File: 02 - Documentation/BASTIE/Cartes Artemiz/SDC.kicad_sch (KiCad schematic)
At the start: 28 parts, among them K1 NO Relay, K10 NO Relay, K11 NO Relay, K2 NO Relay, K3 NO Relay, K4 NO Relay, K5 NC Relay, K6 NO Relay, K7 NO Relay, K8 NO Relay, K9 NO Relay, Q1 NMOS SQ2348ES-T1_GE3, Q2 NMOS SQ2348ES-T1_GE3, Q3 NMOS SQ2348ES-T1_GE3, Q4 NMOS SQ2348ES-T1_GE3, Q5 NMOS SQ2348ES-T1_GE3, Q6 NMOS SQ2348ES-T1_GE3, Q7 NMOS SQ2348ES-T1_GE3, U1 ADG417BR, U2 ADG417BR, U3 ADG417BR, U4 ADG417BR, U5 ADG417BR, U6 ADG417BR, U7 ADG417BR, U8 ADG417BR

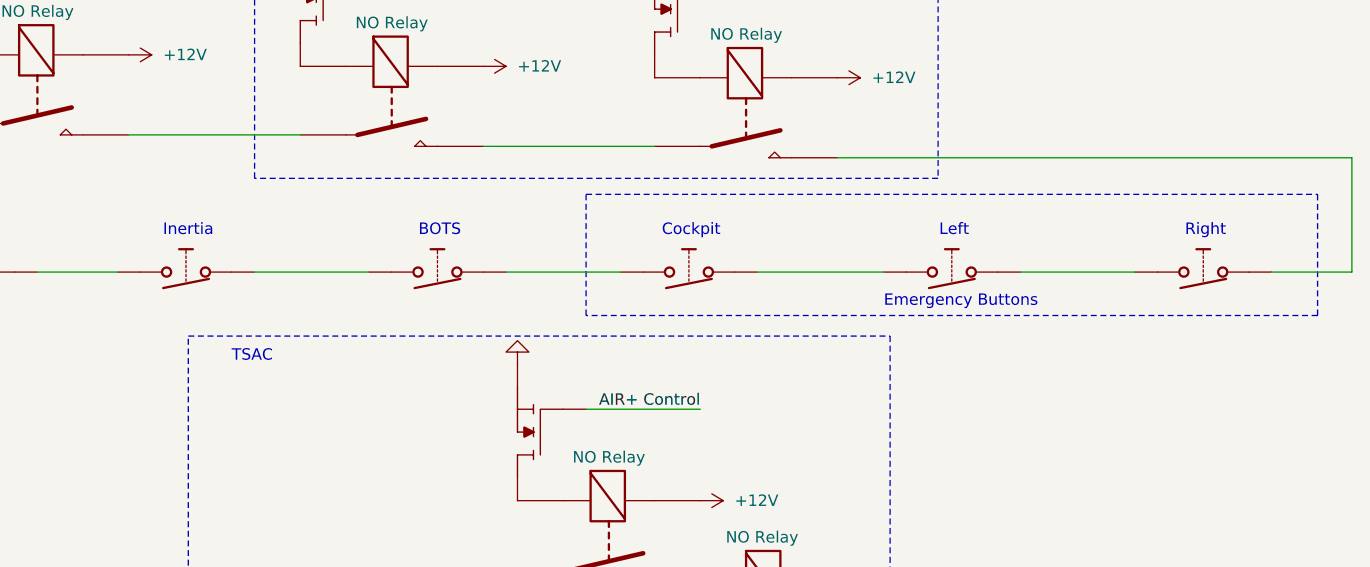
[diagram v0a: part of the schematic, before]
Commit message: Modifications de cartes pour l'ESF
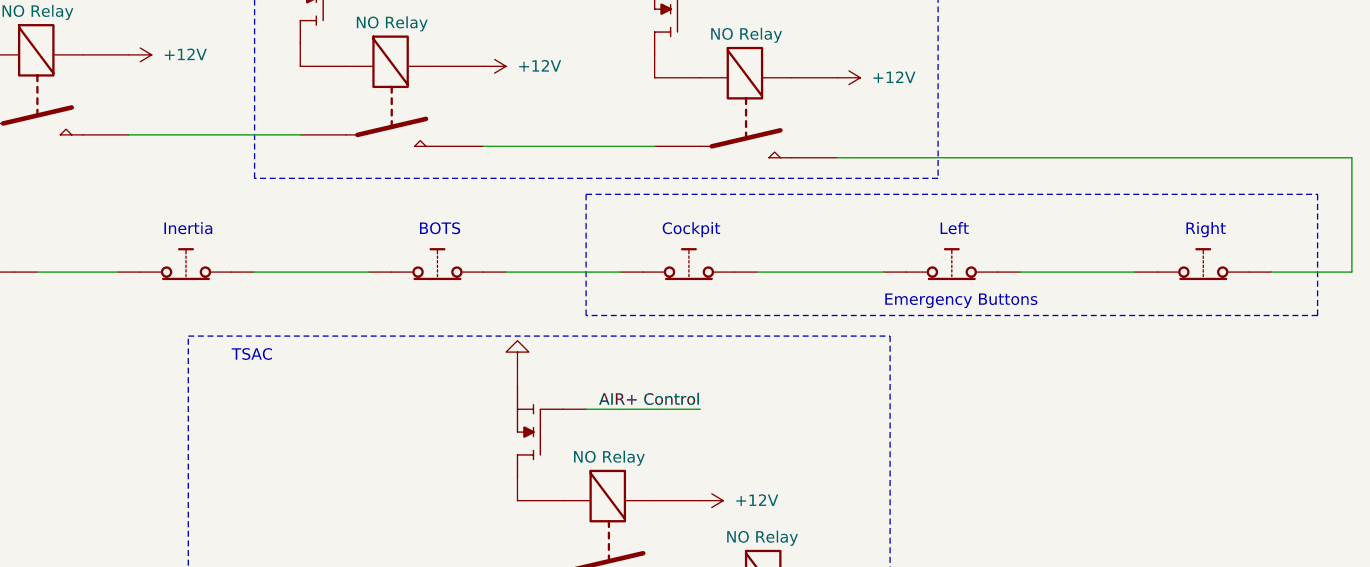
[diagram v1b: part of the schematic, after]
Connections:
- net at U2.: now also U3.; no longer K3.
- net at U5.: now also U6.; no longer U4.
- net at U6.: now also U8.; no longer U5.
- new net: K4., Q4.
- new net: K4., U7., U8.
- new net: K4., K5.
- new net: K1., Q1.
- new net: K1., K2.
- new net: K6., Q5.
- new net: K8., Q7.
- new net: K10., K7.
- new net: K2., K3.
- new net: K3., U4.
- new net: K3., Q3.
- new net: K6., K7., K8., U7.
- new net: U2., U5.
- new net: K6., K9.
- new net: K11., K8.
- new net: K2., Q2.
- new net: K7., Q6.

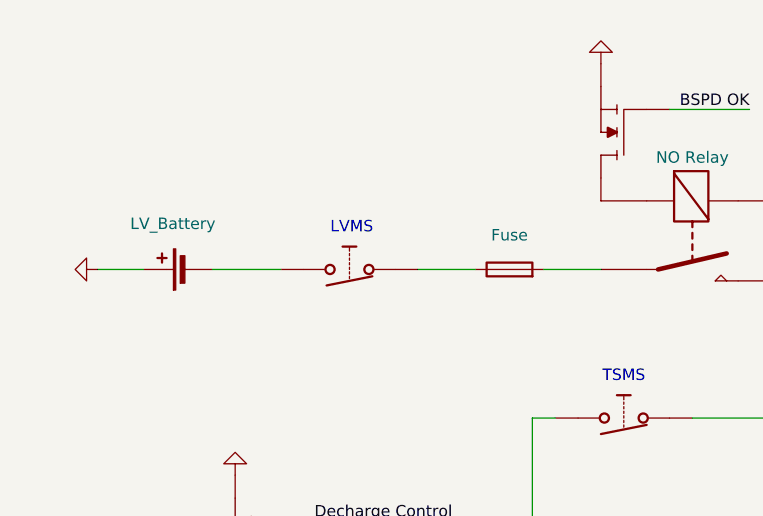
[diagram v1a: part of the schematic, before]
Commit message: Modifications cartes
Prise en compte des retours ECT + PCBs
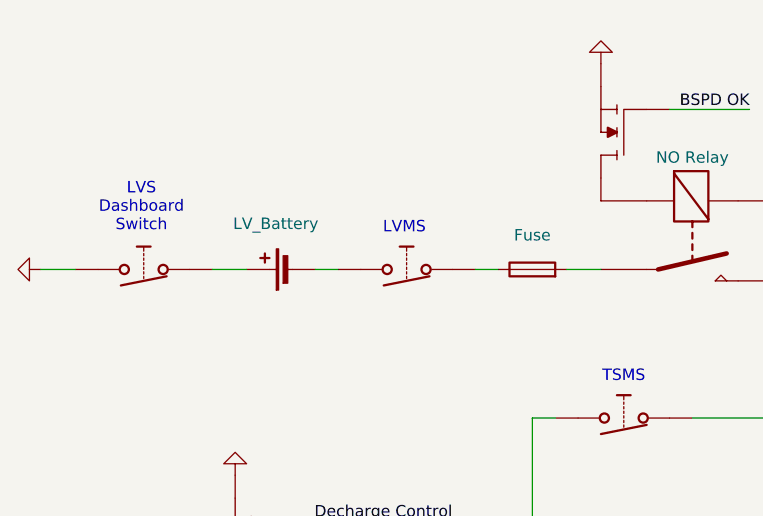
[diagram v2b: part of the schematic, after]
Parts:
- added U9: ADG417BR, Package_SO:SOIC-8_3.9x4.9mm_P1.27mm, symbol Analog_Switch:ADG417BR
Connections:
- net GND: now also U9.; no longer BT1.1 (+)
- net at U4.: now also U3.; no longer K3.
- net at U5.: now also U6.; no longer U2.
- net at U6.: now also U8.; no longer U5.
- net at U3.: now also U2.; no longer U4.
- new net: K4., Q4.
- new net: K4., U7., U8.
- new net: K4., K5.
- new net: K1., Q1.
- new net: K1., K2.
- new net: K6., Q5.
- new net: K8., Q7.
- new net: K10., K7.
- new net: K2., K3.
- new net: K3., U4.
- new net: K3., Q3.
- new net: K6., K7., K8., U7.
- new net: U2., U5.
- new net: K6., K9.
- new net: K11., K8.
- new net: BT1.1 (+), U9.
- new net: K2., Q2.
- new net: K7., Q6.
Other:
- note added: "LVS Dashboard Switch"
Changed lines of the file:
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@@
 	(wire
 		(pts
-			(xy 36.83 46.99) (xy 41.91 46.99)
+			(xy 30.48 46.99) (xy 34.29 46.99)
 		)
 		(stroke
@@
 	(wire
 		(pts
+			(xy 49.53 46.99) (xy 53.34 46.99)
+		)
+		(stroke
+			(width 0)
+			(type default)
+		)
+	)
+	(wire
+		(pts
 			(xy 87.63 63.5) (xy 85.09 63.5)
 		)
@@
 	(wire
 		(pts
-			(xy 86.36 46.99) (xy 92.71 46.99)
+			(xy 88.9 46.99) (xy 92.71 46.99)
 		)
 		(stroke
@@
 	(wire
 		(pts
-			(xy 72.39 46.99) (xy 78.74 46.99)
+			(xy 78.74 46.99) (xy 81.28 46.99)
 		)
 		(stroke
@@
 	(wire
 		(pts
-			(xy 49.53 46.99) (xy 57.15 46.99)
+			(xy 60.96 46.99) (xy 63.5 46.99)
 		)
 		(stroke
@@
 	(text "LVMS"
 		(exclude_from_sim no)
-		(at 65.024 42.418 0)
+		(at 70.866 42.418 0)
 		(effects
 			(font
@@
 		)
 	)
+	(text "LVS\nDashboard\nSwitch"
+		(exclude_from_sim no)
+		(at 41.656 40.132 0)
+		(effects
+			(font
+				(size 1.27 1.27)
+			)
+		)
+	)
 	(text "Left"
 		(exclude_from_sim no)
@@
 	(symbol
 		(lib_id "Device:Fuse")
-		(at 82.55 46.99 90)
+		(at 85.09 46.99 90)
 		(unit 1)
 		(exclude_from_sim no)
@@
 		(fields_autoplaced yes)
 		(property "Reference" "F1"
-			(at 82.55 40.64 90)
+			(at 85.09 40.64 90)
 			(effects
 				(font
@@
 		)
 		(property "Value" "Fuse"
-			(at 82.55 43.18 90)
+			(at 85.09 43.18 90)
 			(effects
 				(font
@@
 		)
 		(property "Footprint" ""
-			(at 82.55 48.768 90)
+			(at 85.09 48.768 90)
 			(effects
 				(font
@@
 		)
 		(property "Datasheet" "~"
-			(at 82.55 46.99 0)
+			(at 85.09 46.99 0)
 			(effects
 				(font
@@
 		)
 		(property "Description" "Fuse"
-			(at 82.55 46.99 0)
+			(at 85.09 46.99 0)
 			(effects
 				(font
@@
 	(symbol
 		(lib_id "power:GND")
-		(at 36.83 46.99 270)
+		(at 30.48 46.99 270)
 		(unit 1)
 		(exclude_from_sim no)
@@
 		(fields_autoplaced yes)
 		(property "Reference" "#PWR01"
-			(at 30.48 46.99 0)
+			(at 24.13 46.99 0)
 			(effects
 				(font
@@
 		)
 		(property "Value" "GND"
-			(at 33.02 46.9899 90)
+			(at 26.67 46.9899 90)
 			(effects
 				(font
@@
 		)
 		(property "Footprint" ""
-			(at 36.83 46.99 0)
+			(at 30.48 46.99 0)
 			(effects
 				(font
@@
 		)
 		(property "Datasheet" ""
-			(at 36.83 46.99 0)
+			(at 30.48 46.99 0)
 			(effects
 				(font
@@
 		)
 		(property "Description" "Power symbol creates a global label with name \"GND\" , ground"
-			(at 36.83 46.99 0)
+			(at 30.48 46.99 0)
 			(effects
 				(font
@@
 	(symbol
 		(lib_id "Device:Battery_Cell")
-		(at 46.99 46.99 90)
+		(at 58.42 46.99 90)
 		(unit 1)
 		(exclude_from_sim no)
@@
 		(fields_autoplaced yes)
 		(property "Reference" "BT1"
-			(at 45.1485 39.37 90)
+			(at 56.5785 39.37 90)
 			(effects
 				(font
@@
 		)
 		(property "Value" "LV_Battery"
-			(at 45.1485 41.91 90)
+			(at 56.5785 41.91 90)
 			(effects
 				(font
@@
 		)
 		(property "Footprint" ""
-			(at 45.466 46.99 90)
+			(at 56.896 46.99 90)
 			(effects
 				(font
@@
 		)
 		(property "Datasheet" "~"
-			(at 45.466 46.99 90)
+			(at 56.896 46.99 90)
 			(effects
 				(font
@@
 		)
 		(property "Description" "Single-cell battery"
-			(at 46.99 46.99 0)
+			(at 58.42 46.99 0)
 			(effects
 				(font
@@
 	)
 	(symbol
+		(lib_name "Analog_Switch:ADG417BR")
 		(lib_id "Analog_Switch:ADG417BR")
-		(at 64.77 46.99 180)
+		(at 71.12 46.99 180)
 		(unit 1)
 		(exclude_from_sim no)
@@
 		(fields_autoplaced yes)
 		(property "Reference" "U1"
-			(at 64.77 50.8 0)
+			(at 71.12 50.8 0)
 			(effects
 				(font
@@
 		)
 		(property "Value" "ADG417BR"
-			(at 64.77 52.07 0)
+			(at 71.12 52.07 0)
 			(effects
 				(font
@@
 		)
 		(property "Footprint" "Package_SO:SOIC-8_3.9x4.9mm_P1.27mm"
-			(at 64.262 36.322 0)
+			(at 70.612 36.322 0)
 			(effects
 				(font
@@
 		)
 		(property "Datasheet" "https://www.analog.com/media/en/technical-documentation/data-sheets/ADG417.pdf"
-			(at 64.77 46.99 0)
+			(at 71.12 46.99 0)
 			(effects
 				(font
@@
 		)
 		(property "Description" "Single SPST Monolithic LC²MOS Analog Switch, normally OFF, 25Ohm Ron, SOIC-8"
-			(at 64.77 46.99 0)
+			(at 71.12 46.99 0)
 			(effects
 				(font
@@
 					(unit 1)
 				)
+			)
+		)
+	)
+	(symbol
+		(lib_name "Analog_Switch:ADG417BR")
+		(lib_id "Analog_Switch:ADG417BR")
+		(at 41.91 46.99 180)
+		(unit 1)
+		(exclude_from_sim no)
+		(in_bom yes)
+		(on_board yes)
+		(dnp no)
+		(fields_autoplaced yes)
+		(property "Reference" "U9"
+			(at 41.91 50.8 0)
+			(effects
+				(font
+					(size 1.27 1.27)
+				)
+				(hide yes)
+			)
+		)
+		(property "Value" "ADG417BR"
+			(at 41.91 52.07 0)
+			(effects
+				(font
+					(size 1.27 1.27)
+				)
+				(hide yes)
+			)
+		)
+		(property "Footprint" "Package_SO:SOIC-8_3.9x4.9mm_P1.27mm"
+			(at 41.402 36.322 0)
+			(effects
+				(font
+					(size 1.27 1.27)
+				)
+				(hide yes)
+			)
+		)
+		(property "Datasheet" "https://www.analog.com/media/en/technical-documentation/data-sheets/ADG417.pdf"
+			(at 41.91 46.99 0)
+			(effects
+				(font
+					(size 1.27 1.27)
+				)
+				(hide yes)
+			)
+		)
+		(property "Description" "Single SPST Monolithic LC²MOS Analog Switch, normally OFF, 25Ohm Ron, SOIC-8"
+			(at 41.91 46.99 0)
+			(effects
+				(font
+					(size 1.27 1.27)
+				)
+				(hide yes)
+			)
+		)
+		(pin ""
+		)
+		(pin "4"
+		)
+		(pin "2"
+		)
+		(pin "5"
+		)
+		(pin "3"
+		)
+		(pin ""
+		)
+		(pin "7"
+		)
+		(instances
+			(project "SDC"
+				(path "/517051b6-4db9-459f-9eb8-ac2447aa7de0"
+					(reference "U9")
+					(unit 1)
+				)
